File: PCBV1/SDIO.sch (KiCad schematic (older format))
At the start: 0 parts

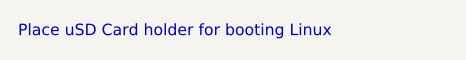
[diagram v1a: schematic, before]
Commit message: Finished video signals, added HDMI and SD connectors.
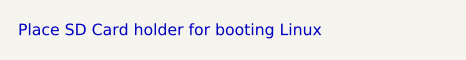
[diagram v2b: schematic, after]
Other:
- note added: "Place SD Card holder for booting Linux"
- note removed: "Place uSD Card holder for booting Linux"
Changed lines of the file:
@@
 $EndDescr
 Text Notes 4850 3050 0    50   ~ 0
-Place uSD Card holder for booting Linux
+Place SD Card holder for booting Linux
 $EndSCHEMATC
